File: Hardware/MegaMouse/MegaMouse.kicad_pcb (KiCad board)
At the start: 2 copper layers, 93.1 x 158.2 mm, 87 parts, among them J101 SHIFT_CONN, J102 PROG_CONN, J103 SHIFT_CONN, J104 PROG_CONN, J201 Motor, J301 Motor, J401 ICSP, J601 USBC, SW401 RESET, SW402 START/MODE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

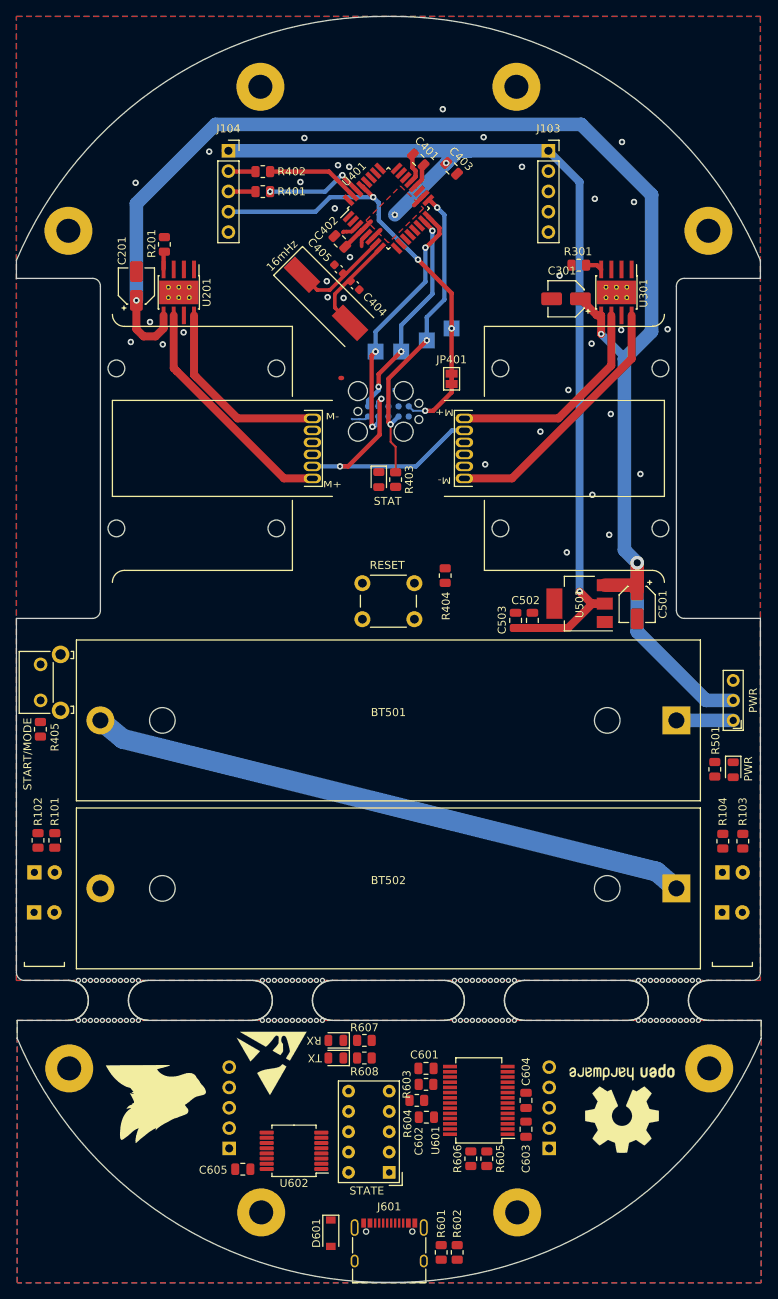
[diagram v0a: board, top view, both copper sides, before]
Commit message: Add IR sensor
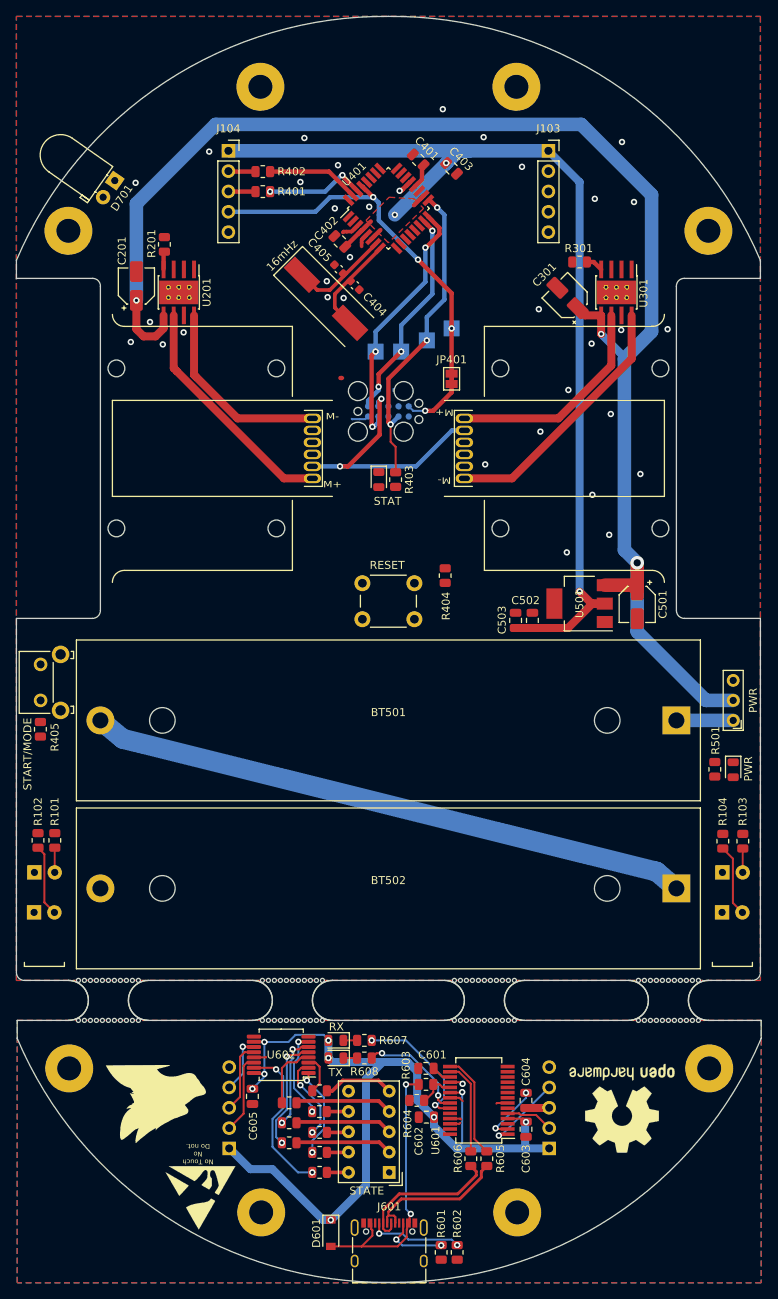
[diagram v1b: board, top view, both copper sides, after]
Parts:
- added D701: D_Photo, LED_THT:LED_D5.0mm_Horizontal_O1.27mm_Z3.0mm_IRBlack, F.Cu at (-34.2, -33.5)
- added R609: 1K, Resistor_SMD:R_0805_2012Metric, F.Cu at (-8.60, 90.5)
- added R610: 1K, Resistor_SMD:R_0805_2012Metric, F.Cu at (-8.60, 85.5)
- added R611: 1K, Resistor_SMD:R_0805_2012Metric, F.Cu at (-12.4, 81.8)
- added R612: 1K, Resistor_SMD:R_0805_2012Metric, F.Cu at (-12.4, 84.3)
- added R613: 1K, Resistor_SMD:R_0805_2012Metric, F.Cu at (-8.60, 88.0)
- added R614: 1K, Resistor_SMD:R_0805_2012Metric, F.Cu at (-8.60, 80.3)
- added R615: 1K, Resistor_SMD:R_0805_2012Metric, F.Cu at (-12.4, 86.8)
- added R616: 1K, Resistor_SMD:R_0805_2012Metric, F.Cu at (-8.62, 82.9)
- moved REF** 19.0 mm to (-23.5, 93.7)
- moved U602 12.1 mm to (-13.4, 75.8)
- moved C605 9.18 mm to (-17.0, 81.0), turned to -90 degrees
- moved R301 0.41 mm to (23.9, -23.3)
- moved C301 0.22 mm to (22.4, -18.8), turned to 135 degrees
- turned R606 to -90 degrees
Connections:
- U602 pad 1: /Upper Board/SEG_B -> Net-(U602-Pad1)
- U602 pad 15: /Upper Board/SEG_A -> Net-(U602-Pad15)
- U602 pad 2: /Upper Board/SEG_C -> Net-(U602-Pad2)
- U602 pad 3: /Upper Board/SEG_D -> Net-(U602-Pad3)
- U602 pad 4: /Upper Board/SEG_E -> Net-(U602-Pad4)
- U602 pad 5: /Upper Board/SEG_F -> Net-(U602-Pad5)
- U602 pad 6: /Upper Board/SEG_G -> Net-(U602-Pad6)
- U602 pad 7: /Upper Board/SEG_DP -> Net-(U602-Pad7)
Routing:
- net +5V: track 166.1 -> 275.0 mm, vias 5 -> 14
- net VBUS: track 0.00 -> 34.5 mm, vias 0 -> 2
- net Net-(U602-Pad15): track 0.00 -> 19.8 mm, vias 0 -> 2
- net /Upper Board/USB-: track 0.00 -> 19.2 mm
- net /Upper Board/USB+: track 0.00 -> 18.4 mm
- net Net-(R607-Pad1): track 0.00 -> 16.9 mm, vias 0 -> 2
- net Net-(U602-Pad5): track 0.00 -> 14.6 mm, vias 0 -> 2
- net Net-(R608-Pad2): track 0.00 -> 13.8 mm, vias 0 -> 2
- net Net-(R605-Pad2): track 0.00 -> 13.1 mm
- net /Upper Board/SEG_E: track 0.00 -> 12.2 mm
- net /Upper Board/SEG_G: track 0.00 -> 12.1 mm
- net /Upper Board/SEG_F: track 0.00 -> 12.1 mm
- net Net-(U602-Pad6): track 0.00 -> 11.8 mm, vias 0 -> 2
- net Net-(R606-Pad1): track 0.00 -> 11.7 mm
- net Net-(J601-PadA5): track 0.00 -> 11.7 mm, vias 0 -> 2
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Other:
- board text added: "No Touch No Do not."

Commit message: Add silkscreen!
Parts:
- removed D401: STAT, LED_SMD:LED_0805_2012Metric
- removed the R403 at (0.90, 3.90)
- added G***: LOGO, MegaMouse:MegaMouseLogo, B.Cu at (0.00, -30.0)
- added JP101: BrakeBridge, Jumper:SolderJumper-2_P1.3mm_Bridged_Pad1.0x1.5mm, F.Cu at (-0.20, 1.30)
- added Stripes: Stripes, MegaMouse:Stripes, F.Cu at (0.70, 65.0)
- added Stripes: Stripes, MegaMouse:Stripes, F.Cu at (16.7, 65.0)
- added Stripes: Stripes, MegaMouse:Stripes, F.Cu at (32.7, 65.0)
- added Stripes: Stripes, MegaMouse:Stripes, F.Cu at (8.70, 65.0)
- added Stripes: Stripes, MegaMouse:Stripes, F.Cu at (-23.3, 65.0)
- added Stripes: Stripes, MegaMouse:Stripes, F.Cu at (-7.30, 65.0)
- added Stripes: Stripes, MegaMouse:Stripes, F.Cu at (-15.3, 65.0)
- added Stripes: Stripes, MegaMouse:Stripes, F.Cu at (-31.3, 65.0)
- added Stripes: Stripes, MegaMouse:Stripes, F.Cu at (24.7, 65.0)
- moved G*** 52.9 mm to (-23.2, -5.70)
- moved REF** 48.4 mm to (23.9, -0.30)
- moved D501 0.06 mm to (43.1, 40.1)
- renumbered R404 to R403, R405 to R404
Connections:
- R101 pad 2: unconnected-(R101-Pad2) -> /L_TURN
- R102 pad 2: unconnected-(R102-Pad2) -> /BRAKE
- R103 pad 2: unconnected-(R103-Pad2) -> /R_TURN
- R104 pad 2: unconnected-(R104-Pad2) -> /BRAKE
- U401 pad 10: unconnected-(U401-Pad10) -> /L_TURN
- U401 pad 11: unconnected-(U401-Pad11) -> /R_TURN
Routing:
- net /BRAKE: track 0.00 -> 136.1 mm
- net +5V: track 275.0 -> 373.2 mm
- net /R_TURN: track 0.00 -> 84.5 mm
- net /L_TURN: track 0.00 -> 80.8 mm
- net /MCU/RST: track 46.9 -> 53.4 mm
- net /MCU/START/MODE: track 0.00 -> 2.71 mm
- net Net-(D501-Pad2): track 0.00 -> 2.31 mm
- net /MCU/SCK: track 39.8 -> 37.9 mm
- net GND: vias 35 -> 43
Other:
- board text added: "${FULL_REVISION}"
- board text added: "Battery Goes here."
- board text removed: "MegaMouse ${FULL_REVISION}"

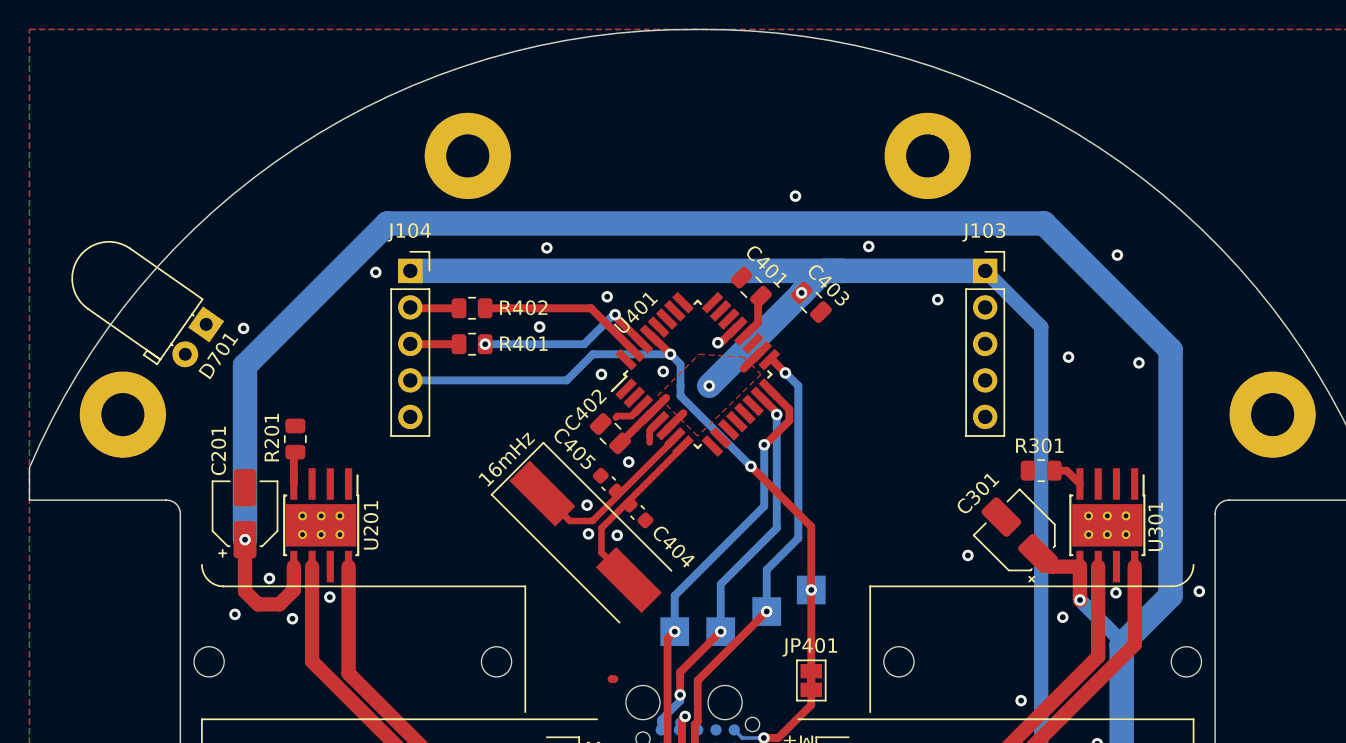
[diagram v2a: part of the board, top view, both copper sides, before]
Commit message: Add inital photodiodes
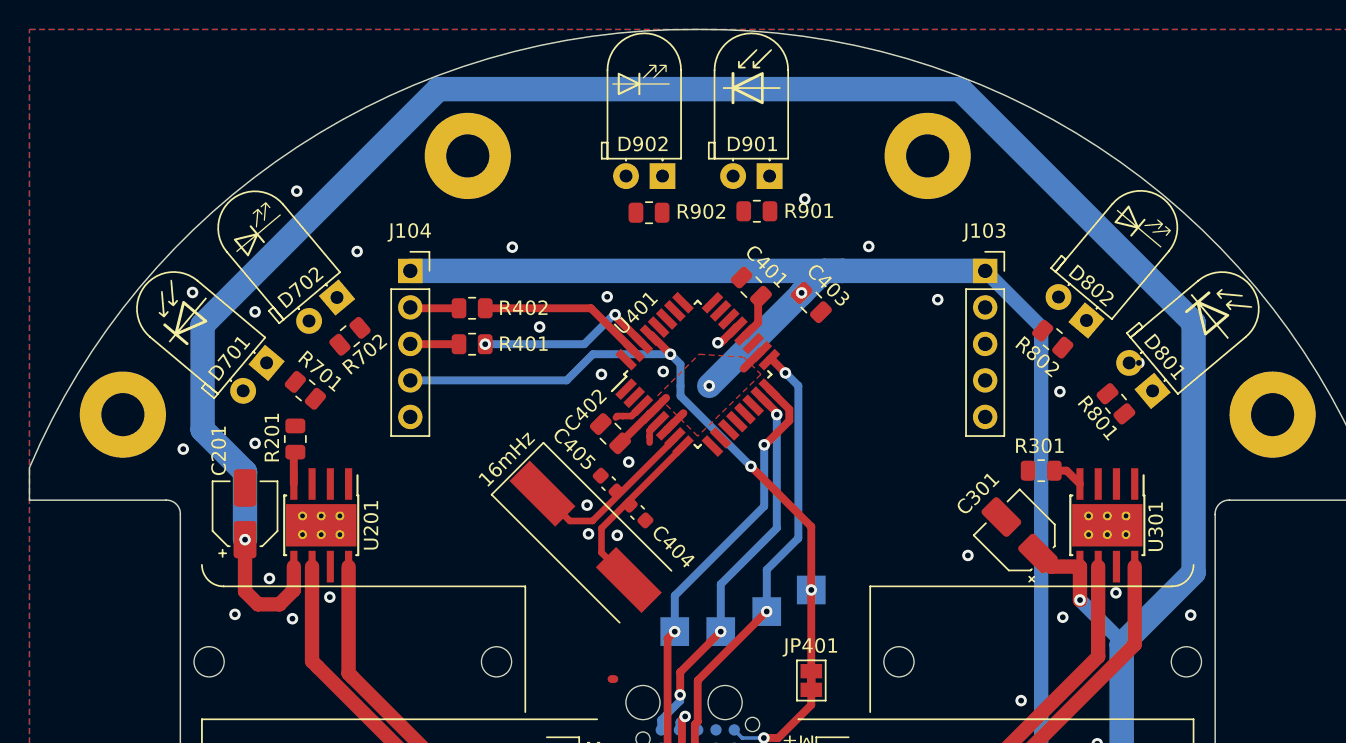
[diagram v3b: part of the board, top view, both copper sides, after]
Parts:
- added D702: IR_LED, LED_THT:LED_D5.0mm_Horizontal_O1.27mm_Z3.0mm_Clear, F.Cu at (-25.1, -35.4)
- added D801: PhotoDiode, LED_THT:LED_D5.0mm_Horizontal_O1.27mm_Z3.0mm_IRBlack, F.Cu at (31.6, -28.9)
- added D802: IR_LED, LED_THT:LED_D5.0mm_Horizontal_O1.27mm_Z3.0mm_Clear, F.Cu at (27.1, -33.8)
- added D901: PhotoDiode, LED_THT:LED_D5.0mm_Horizontal_O1.27mm_Z3.0mm_IRBlack, F.Cu at (5.00, -43.8)
- added D902: IR_LED, LED_THT:LED_D5.0mm_Horizontal_O1.27mm_Z3.0mm_Clear, F.Cu at (-2.45, -43.8)
- added G***: LOGO, MegaMouse:PhotoDiodeLOGO, F.Cu at (-36.1, -34.4)
- added G***: LOGO, MegaMouse:LEDLOGO, F.Cu at (-30.8, -40.0)
- added G***: LOGO, MegaMouse:LEDLOGO, F.Cu at (-3.95, -50.5)
- added G***: LOGO, MegaMouse:PhotoDiodeLOGO, F.Cu at (3.75, -50.8)
- added G***: LOGO, MegaMouse:LEDLOGO, F.Cu at (30.9, -40.4)
- added G***: LOGO, MegaMouse:PhotoDiodeLOGO, F.Cu at (36.3, -34.6)
- added R701: 10K, Resistor_SMD:R_0805_2012Metric, F.Cu at (-27.3, -28.9)
- added R702: 10K, Resistor_SMD:R_0805_2012Metric, F.Cu at (-24.2, -32.6)
- added R801: 10K, Resistor_SMD:R_0805_2012Metric, F.Cu at (29.1, -27.9)
- added R802: 10K, Resistor_SMD:R_0805_2012Metric, F.Cu at (24.7, -32.5)
- added R901: 10K, Resistor_SMD:R_0805_2012Metric, F.Cu at (4.11, -41.4)
- added R902: 10K, Resistor_SMD:R_0805_2012Metric, F.Cu at (-3.39, -41.2)
- D701: value D_Photo -> PhotoDiode
- moved D701 4.98 mm to (-30.0, -30.8), turned to -130 degrees
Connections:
- D701 pad 1: unconnected-(D701-Pad1) -> /LIR
- D701 pad 2: unconnected-(D701-Pad2) -> GND
- U401 pad 1: unconnected-(U401-Pad1) -> /ENABLE
- U401 pad 23: unconnected-(U401-Pad23) -> /LIR
- U401 pad 24: unconnected-(U401-Pad24) -> /FRNT
- U401 pad 25: unconnected-(U401-Pad25) -> /RIR
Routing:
- net +BATT: track 183.5 -> 200.5 mm
- net GND: vias 43 -> 46

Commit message: Add in some more, random junk
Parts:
- removed the C403 at (7.90, -35.0)
- removed JP101: BrakeBridge, Jumper:SolderJumper-2_P1.3mm_Bridged_Pad1.0x1.5mm
- added C405: 100nF, Capacitor_SMD:C_0805_2012Metric, F.Cu at (9.50, -23.8)
- added RV701: 10K, Potentiometer_SMD:Potentiometer_Bourns_TC33X_Vertical, F.Cu at (-23.7, -27.9)
- added RV801: 10K, Potentiometer_SMD:Potentiometer_Bourns_TC33X_Vertical, F.Cu at (25.9, -27.1)
- added RV901: 10K, Potentiometer_SMD:Potentiometer_Bourns_TC33X_Vertical, F.Cu at (8.70, -40.5)
- added TP405: TestPoint, TestPoint:TestPoint_Pad_2.0x2.0mm, B.Cu at (15.6, -21.8)
- added U402: SN74HC595, KenwoodFox:SN74HC595, F.Cu at (14.0, -20.9)
- R701, R801, R901: value 10K -> DNP
- moved JP401 1.82 mm to (6.10, -8.95)
- moved R701 0.31 mm to (-27.6, -28.9)
- turned R702 to -140 degrees
- renumbered C404 to C403, C405 to C404
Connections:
- net /MCU/LATCH_OUT renamed /MCU/LATCH
- D702 pad 1: Net-(D702-Pad1) -> GND
- D702 pad 2: GND -> Net-(R702-Pad2)
- D802 pad 1: Net-(D802-Pad1) -> GND
- D802 pad 2: GND -> Net-(R802-Pad2)
- D902 pad 1: Net-(D902-Pad1) -> GND
- D902 pad 2: GND -> Net-(R902-Pad2)
- J103 pad 4: /MCU/CLOCK_OUT -> /MCU/CLOCK
- J301 pad 3: /RightMotor/EncA -> /MCU/R_ENC_A
- J301 pad 4: /RightMotor/EncB -> /MCU/R_ENC_B
- R702 pad 2: Net-(D702-Pad1) -> Net-(R702-Pad2)
- R802 pad 2: Net-(D802-Pad1) -> Net-(R802-Pad2)
- R902 pad 2: Net-(D902-Pad1) -> Net-(R902-Pad2)
- U301 pad 2: /RightMotor/IN2 -> /MCU/R_MOT_2
- U301 pad 3: /RightMotor/IN1 -> /MCU/R_MOT_1
- U401 pad 1: /ENABLE -> /MCU/R_ENC_A
- U401 pad 10: /L_TURN -> /LeftMotor/IN1
- U401 pad 11: /R_TURN -> /LeftMotor/IN2
- U401 pad 13: /MCU/DATA_OUT -> /MCU/DATA
- U401 pad 2: unconnected-(U401-Pad2) -> /MCU/CLOCK
- U401 pad 26: unconnected-(U401-Pad26) -> /LeftMotor/EncB
- U401 pad 27: unconnected-(U401-Pad27) -> /MCU/R_ENC_B
- U401 pad 28: unconnected-(U401-Pad28) -> /MCU/R_MOT_1
- U401 pad 32: /MCU/CLOCK_OUT -> /LeftMotor/EncA
- U401 pad 9: unconnected-(U401-Pad9) -> /MCU/R_MOT_2
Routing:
- net /MCU/START/MODE: track 2.71 -> 67.1 mm
- net /MCU/SCK: track 37.9 -> 34.7 mm
- net /MCU/DATA_OUT: track 0.00 -> 2.80 mm, vias 0 -> 1
- net /MCU/ICSP_RST: track 7.59 -> 6.51 mm
- net +5V: vias 14 -> 13

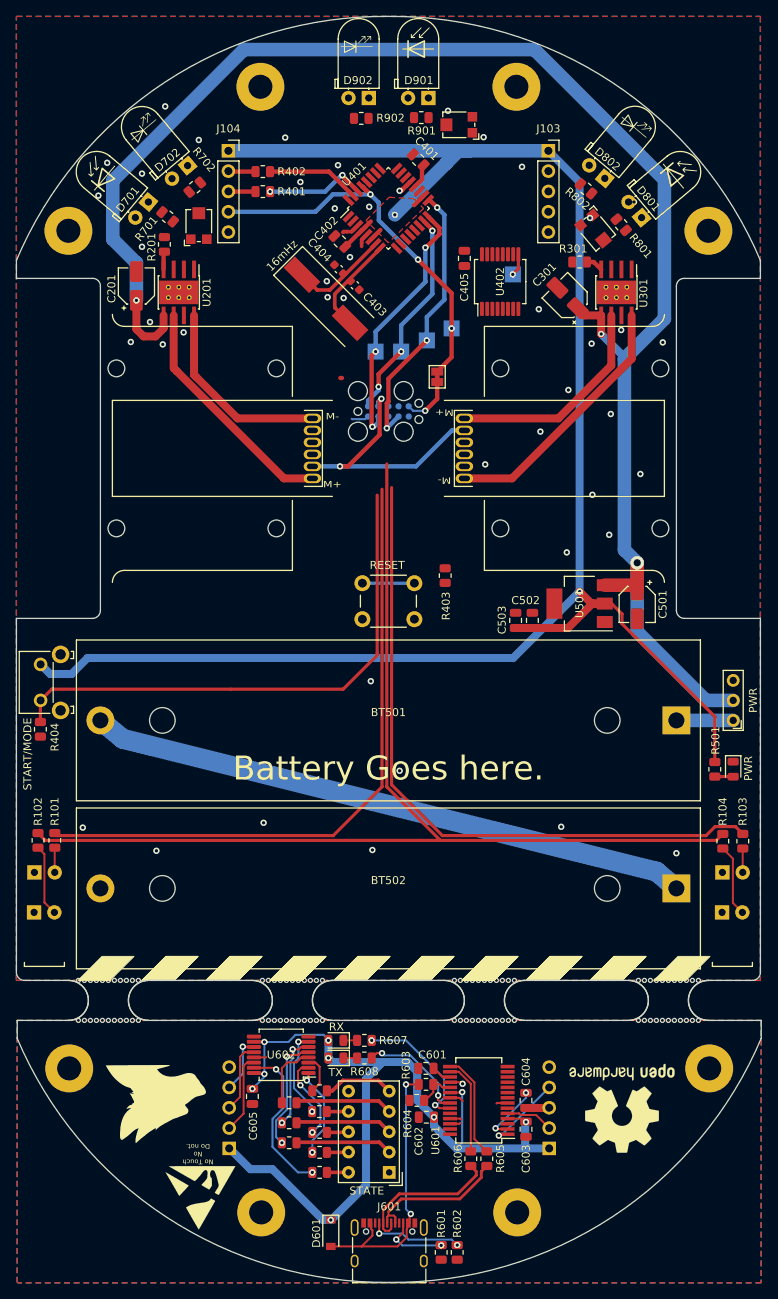
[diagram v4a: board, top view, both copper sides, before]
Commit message: Add lines for enabling emittersg
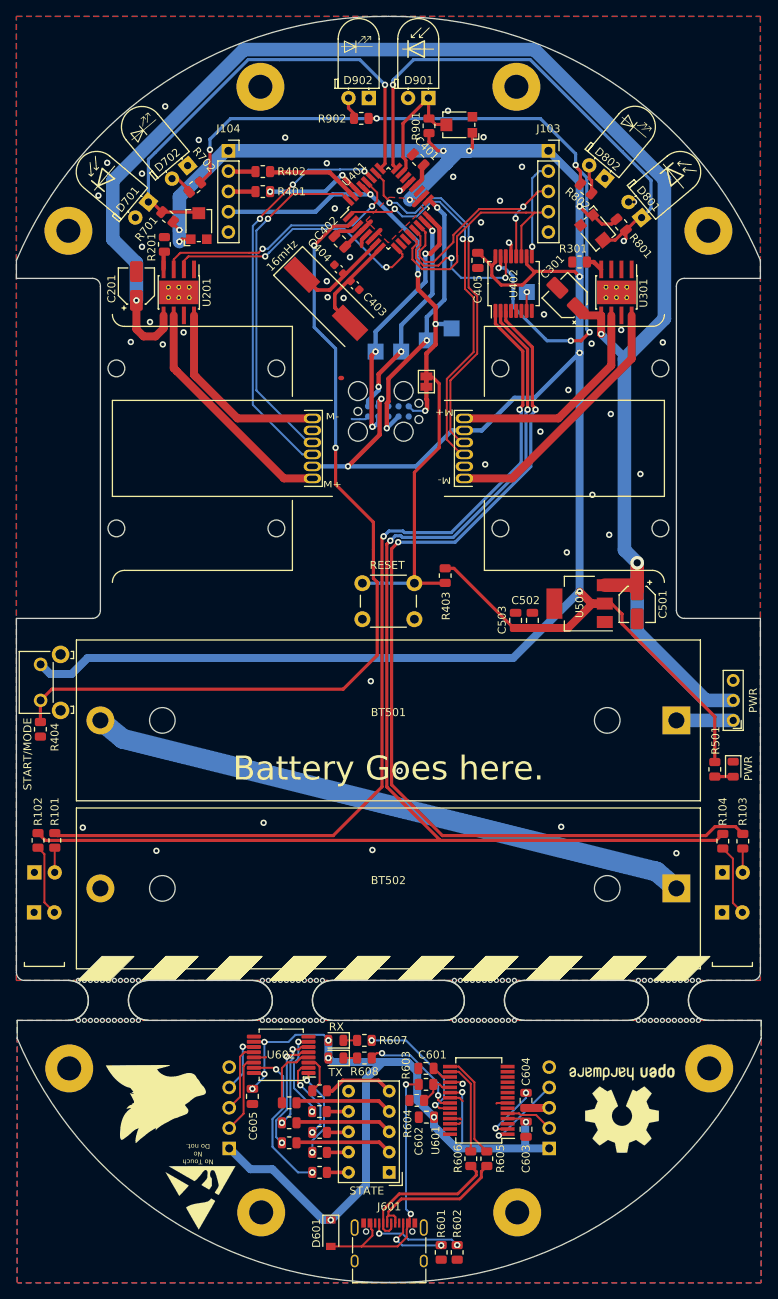
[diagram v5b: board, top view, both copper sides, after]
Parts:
- removed TP405: TestPoint, TestPoint:TestPoint_Pad_2.0x2.0mm
- added G***: LOGO, MegaMouse:MegaMouseQR, B.Cu at (0.00, 31.0)
- added TP406: TestPoint, TestPoint:TestPoint_Pad_2.0x2.0mm, B.Cu at (17.3, -19.6)
- moved G*** 34.0 mm to (-17.8, 27.9)
- moved C405 1.70 mm to (11.2, -23.5)
- moved U402 1.70 mm to (15.7, -20.6)
- moved JP401 1.48 mm to (4.75, -8.35)
- moved R901 1.41 mm to (5.08, -40.3), turned to 90 degrees
- turned R902 to 180 degrees
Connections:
- U401 pad 10: /LeftMotor/IN1 -> /MCU/R_MOT_1
- U401 pad 11: /LeftMotor/IN2 -> /MCU/R_MOT_2
- U401 pad 12: /MCU/START/MODE -> /MCU/CLOCK
- U401 pad 2: /MCU/CLOCK -> /MCU/START/MODE
- U401 pad 23: /LIR -> /FRNT
- U401 pad 24: /FRNT -> /RIR
- U401 pad 25: /RIR -> /LIR
- U401 pad 26: /LeftMotor/EncB -> /MCU/R_ENC_B
- U401 pad 27: /MCU/R_ENC_B -> /LeftMotor/EncB
- U401 pad 28: /MCU/R_MOT_1 -> /LeftMotor/IN1
- U401 pad 9: /MCU/R_MOT_2 -> /LeftMotor/IN2
- U402 pad 2: /R_TURN -> /BRAKE
- U402 pad 3: /BRAKE -> /R_TURN
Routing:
- net /ENABLE: track 0.00 -> 100.5 mm, vias 0 -> 6
- net +5V: track 373.2 -> 448.4 mm, vias 13 -> 20
- net /RIR: track 0.00 -> 63.3 mm, vias 0 -> 2
- net /LIR: track 0.00 -> 59.0 mm, vias 0 -> 1
- net /LeftMotor/EncB: track 0.00 -> 50.6 mm, vias 0 -> 3
- net /MCU/R_ENC_A: track 0.00 -> 49.0 mm, vias 0 -> 2
- net /MCU/R_ENC_B: track 0.00 -> 47.1 mm, vias 0 -> 2
- net /LeftMotor/EncA: track 0.00 -> 43.4 mm, vias 0 -> 1
- net /MCU/START/MODE: track 67.1 -> 107.7 mm, vias 0 -> 2
- net /L_TURN: track 80.8 -> 116.8 mm, vias 0 -> 2
- net /R_TURN: track 84.5 -> 119.8 mm, vias 0 -> 2
- net /LeftMotor/IN2: track 0.00 -> 33.9 mm, vias 0 -> 2
- net /MCU/RST: track 53.7 -> 86.7 mm
- net /LeftMotor/IN1: track 0.00 -> 32.6 mm, vias 0 -> 2
- net /BRAKE: track 136.1 -> 168.5 mm, vias 0 -> 2
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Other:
- board text added: "Designed by Joe Sedutto"
- board text added: "With thanks to Arthur Aznive Mark Sedutto"
